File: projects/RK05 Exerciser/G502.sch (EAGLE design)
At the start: 51 parts

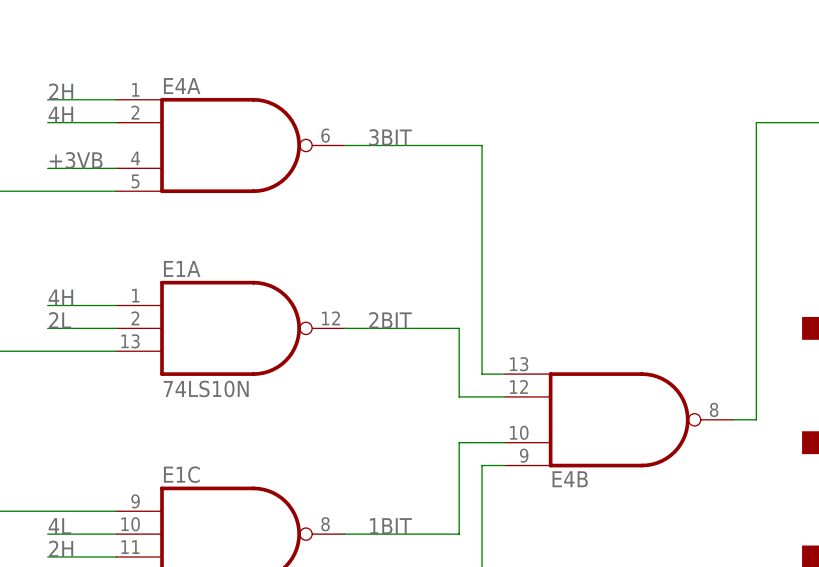
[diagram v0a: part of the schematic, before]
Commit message: Where possible, map 74xx-jameco to 74xx-us. Moved the 7438 to dec-con.lbr. Also changed the spelling of CRYTAL to CRYSTAL.
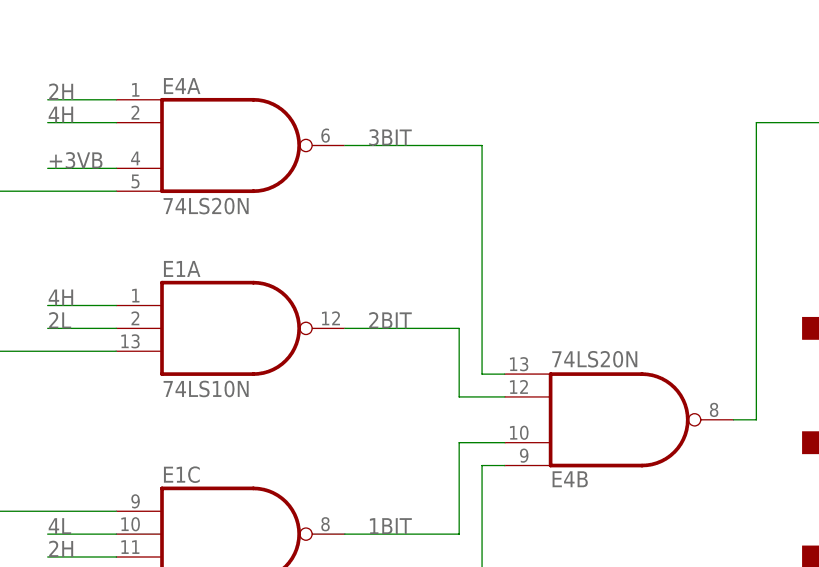
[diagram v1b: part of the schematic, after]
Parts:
- E1: device 74xx-jameco:74LS10N -> 74xx-us:74LS10N
- E10, E7: device 74xx-jameco:74LS00N -> 74xx-us:74LS00N
- E11, E2, E5: device 74xx-jameco:74LS74N -> 74xx-us:74LS74N
- E3: device 74xx-jameco:74LS42N -> 74xx-us:74LS42N
- E4: value (none) -> 74LS20N; device 74xx-jameco:74LS20N -> 74xx-us:74LS20N
- E6: device 74xx-jameco:74LS04N -> 74xx-us:74LS04N
- E8: device 74xx-jameco:74LS123N -> 74xx-us:74LS123N
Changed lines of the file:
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@@
 <part name="V2" library="supply2" deviceset="GND" device=""/>
 <part name="R4" library="rcl" deviceset="R-US_" device="0207/10" value="1K"/>
-<part name="E10" library="74xx-jameco" deviceset="74*00" device="N" technology="LS"/>
-<part name="E11" library="74xx-jameco" deviceset="74*74" device="N" technology="LS"/>
+<part name="E10" library="74xx-us" deviceset="74*00" device="N" technology="LS"/>
+<part name="E11" library="74xx-us" deviceset="74*74" device="N" technology="LS"/>
 <part name="V3" library="supply2" deviceset="VCC" device=""/>
 <part name="R5" library="rcl" deviceset="R-US_" device="0207/10" value="56K"/>
@@
 <part name="R7" library="rcl" deviceset="R-US_" device="0207/10" value="1K"/>
 <part name="V4" library="supply2" deviceset="VCC" device=""/>
-<part name="E8" library="74xx-jameco" deviceset="74*123" device="N" technology="LS"/>
+<part name="E8" library="74xx-us" deviceset="74*123" device="N" technology="LS"/>
 <part name="R2" library="rcl" deviceset="R-US_" device="0207/10" value="5.6k*"/>
 <part name="R1" library="pot" deviceset="TRIM_EU-" device="B90P" value="10K*"/>
 <part name="C13" library="rcl" deviceset="C-US" device="075-032X103" value="47pf"/>
 <part name="C12" library="rcl" deviceset="C-US" device="075-032X103" value="27pf"/>
-<part name="E5" library="74xx-jameco" deviceset="74*74" device="N" technology="LS"/>
-<part name="E2" library="74xx-jameco" deviceset="74*74" device="N" technology="LS"/>
+<part name="E5" library="74xx-us" deviceset="74*74" device="N" technology="LS"/>
+<part name="E2" library="74xx-us" deviceset="74*74" device="N" technology="LS"/>
 <part name="R3" library="rcl" deviceset="R-US_" device="0207/10" value="1K"/>
 <part name="V5" library="supply2" deviceset="VCC" device=""/>
@@
 <part name="V7" library="supply2" deviceset="VCC" device=""/>
 <part name="V8" library="supply2" deviceset="GND" device=""/>
-<part name="E7" library="74xx-jameco" deviceset="74*00" device="N" technology="LS"/>
+<part name="E7" library="74xx-us" deviceset="74*00" device="N" technology="LS"/>
 <part name="R12" library="rcl" deviceset="R-US_" device="0207/10" value="330"/>
 <part name="R13" library="rcl" deviceset="R-US_" device="0207/10" value="330"/>
@@
 <part name="V16" library="supply2" deviceset="GND" device=""/>
 <part name="V17" library="supply2" deviceset="GND" device=""/>
-<part name="E4" library="74xx-jameco" deviceset="74*20" device="N" technology="LS"/>
-<part name="E1" library="74xx-jameco" deviceset="74*10" device="N" technology="LS"/>
+<part name="E4" library="74xx-us" deviceset="74*20" device="N" technology="LS"/>
+<part name="E1" library="74xx-us" deviceset="74*10" device="N" technology="LS"/>
 <part name="SECTOR_SELECT" library="switch" deviceset="CK101X12" device=""/>
-<part name="E3" library="74xx-jameco" deviceset="74*42" device="N" technology="LS"/>
+<part name="E3" library="74xx-us" deviceset="74*42" device="N" technology="LS"/>
 <part name="V18" library="supply2" deviceset="GND" device=""/>
-<part name="E6" library="74xx-jameco" deviceset="74*04" device="N" technology="LS"/>
+<part name="E6" library="74xx-us" deviceset="74*04" device="N" technology="LS"/>
 <part name="R8" library="rcl" deviceset="R-US_" device="0207/10" value="1K"/>
 <part name="V19" library="supply2" deviceset="VCC" device=""/>

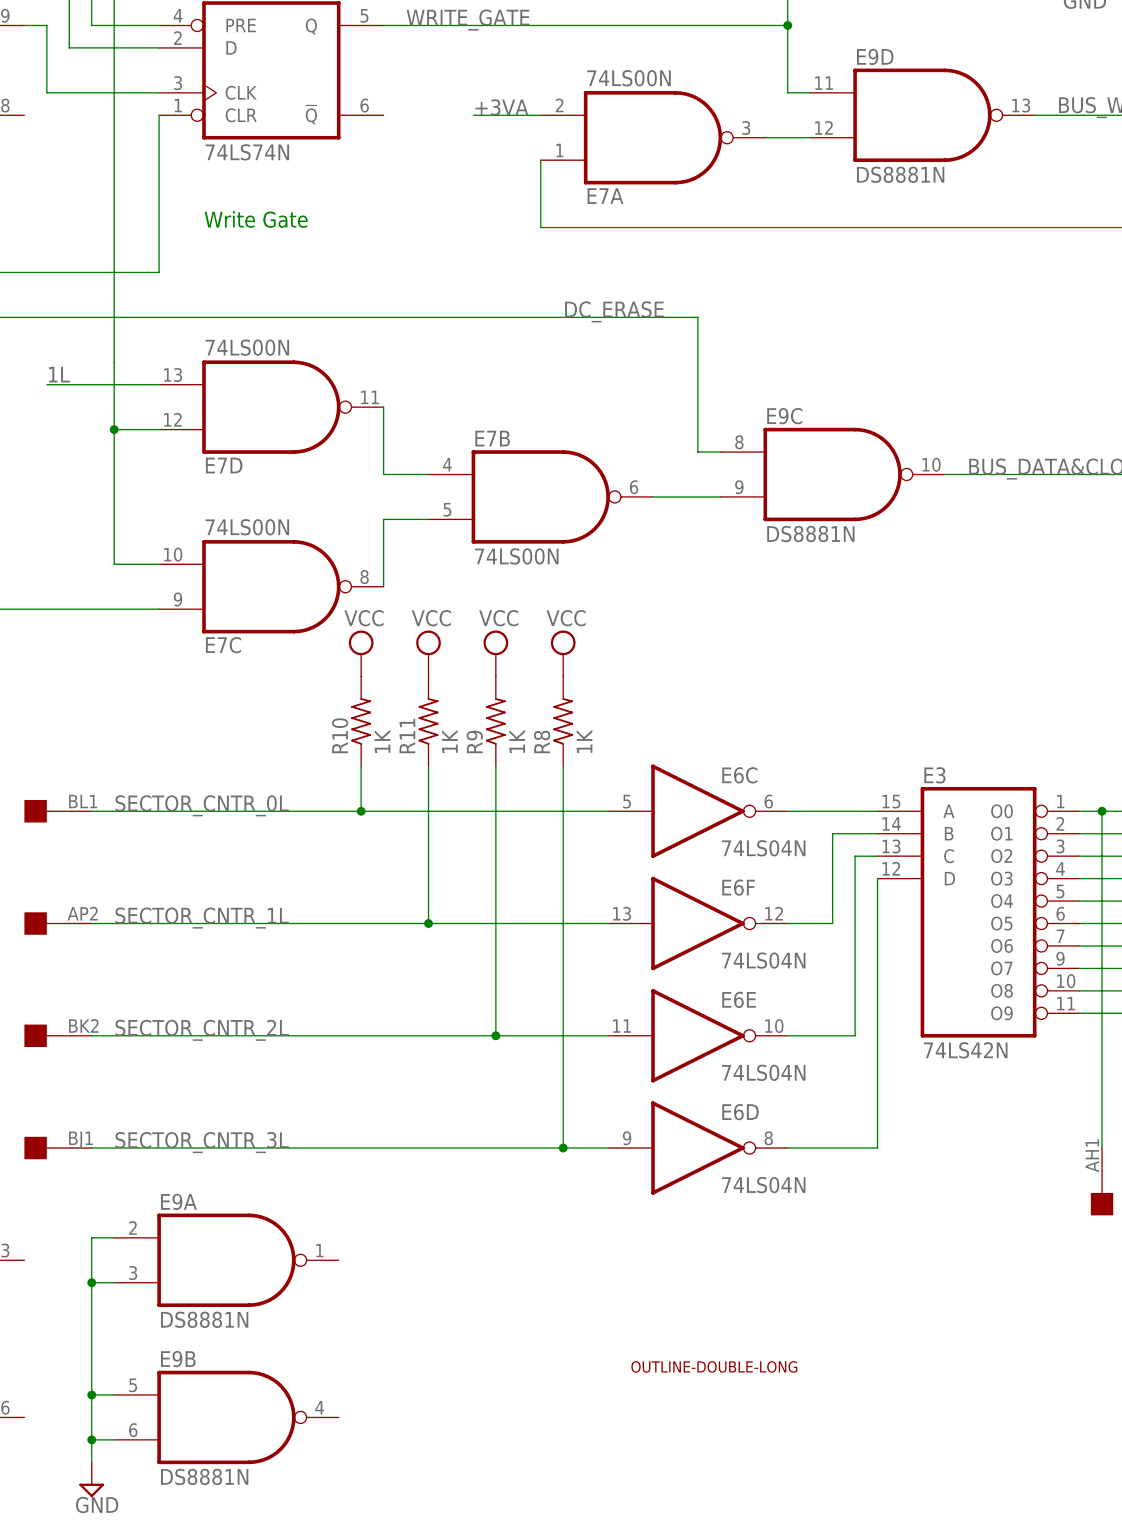
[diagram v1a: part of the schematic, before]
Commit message: Fix references to DS8881 to refer to N8881.
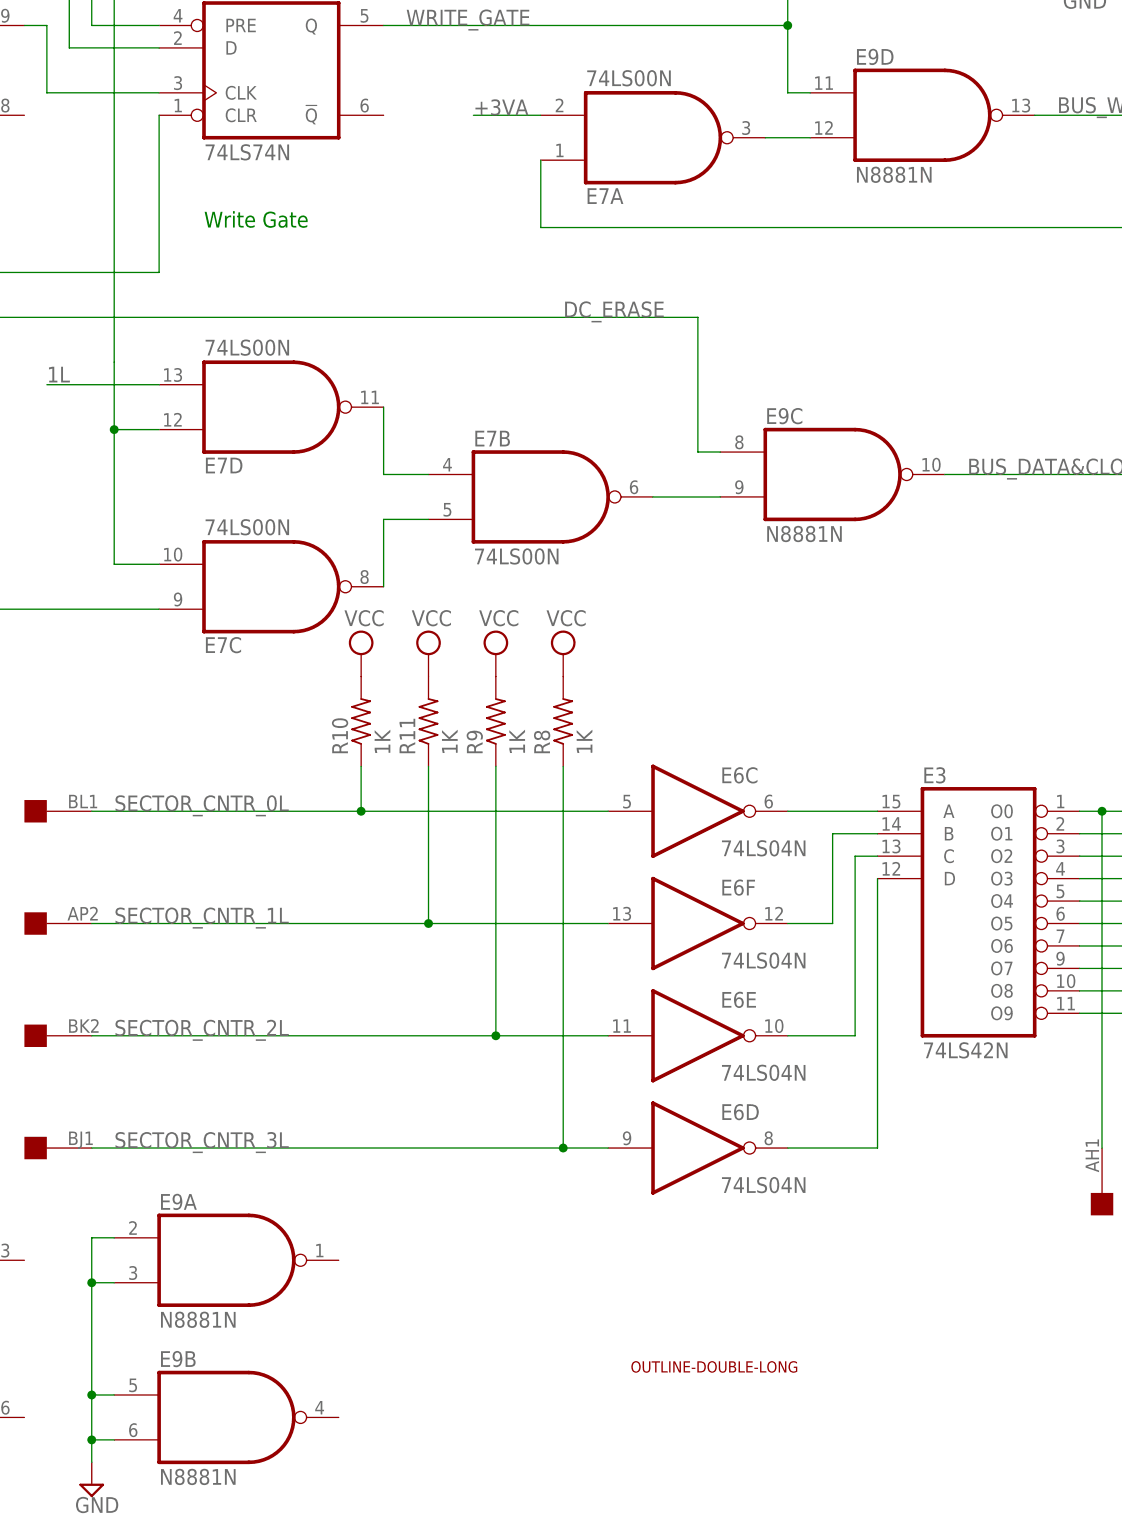
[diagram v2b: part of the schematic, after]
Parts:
- E9: value DS8881N -> N8881N; device dec-con:DS8881N -> dec-con:N8881N
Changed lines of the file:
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@@
 <part name="DC_ERASE" library="switch" deviceset="255SB" device=""/>
 <part name="V13" library="supply2" deviceset="GND" device=""/>
-<part name="E9" library="dec-con" deviceset="DS8881" device="N"/>
+<part name="E9" library="dec-con" deviceset="N8881" device="N"/>
 <part name="BIT3" library="switch" deviceset="255SB" device=""/>
 <part name="BIT1" library="switch" deviceset="255SB" device=""/>
@@
 </sheet>
 </sheets>
+<errors>
+</errors>
 </schematic>
 </drawing>
